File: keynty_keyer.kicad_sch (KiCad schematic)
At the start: 0 parts

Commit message: added power conditioning
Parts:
- added BT1: 9V Alkaline, symbol Device:Battery_Cell
- added C1: 100u, symbol Device:C_Polarized
- added R1: 47, symbol Device:R
- added SW1: Power, symbol Switch:SW_SPST
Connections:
- new net: BT1.1 (+), SW1.1 (A)
- new net: R1.1, SW1.2 (B)
- new net GND: BT1.2 (-), C1.2
- new net VCC: C1.1, R1.2

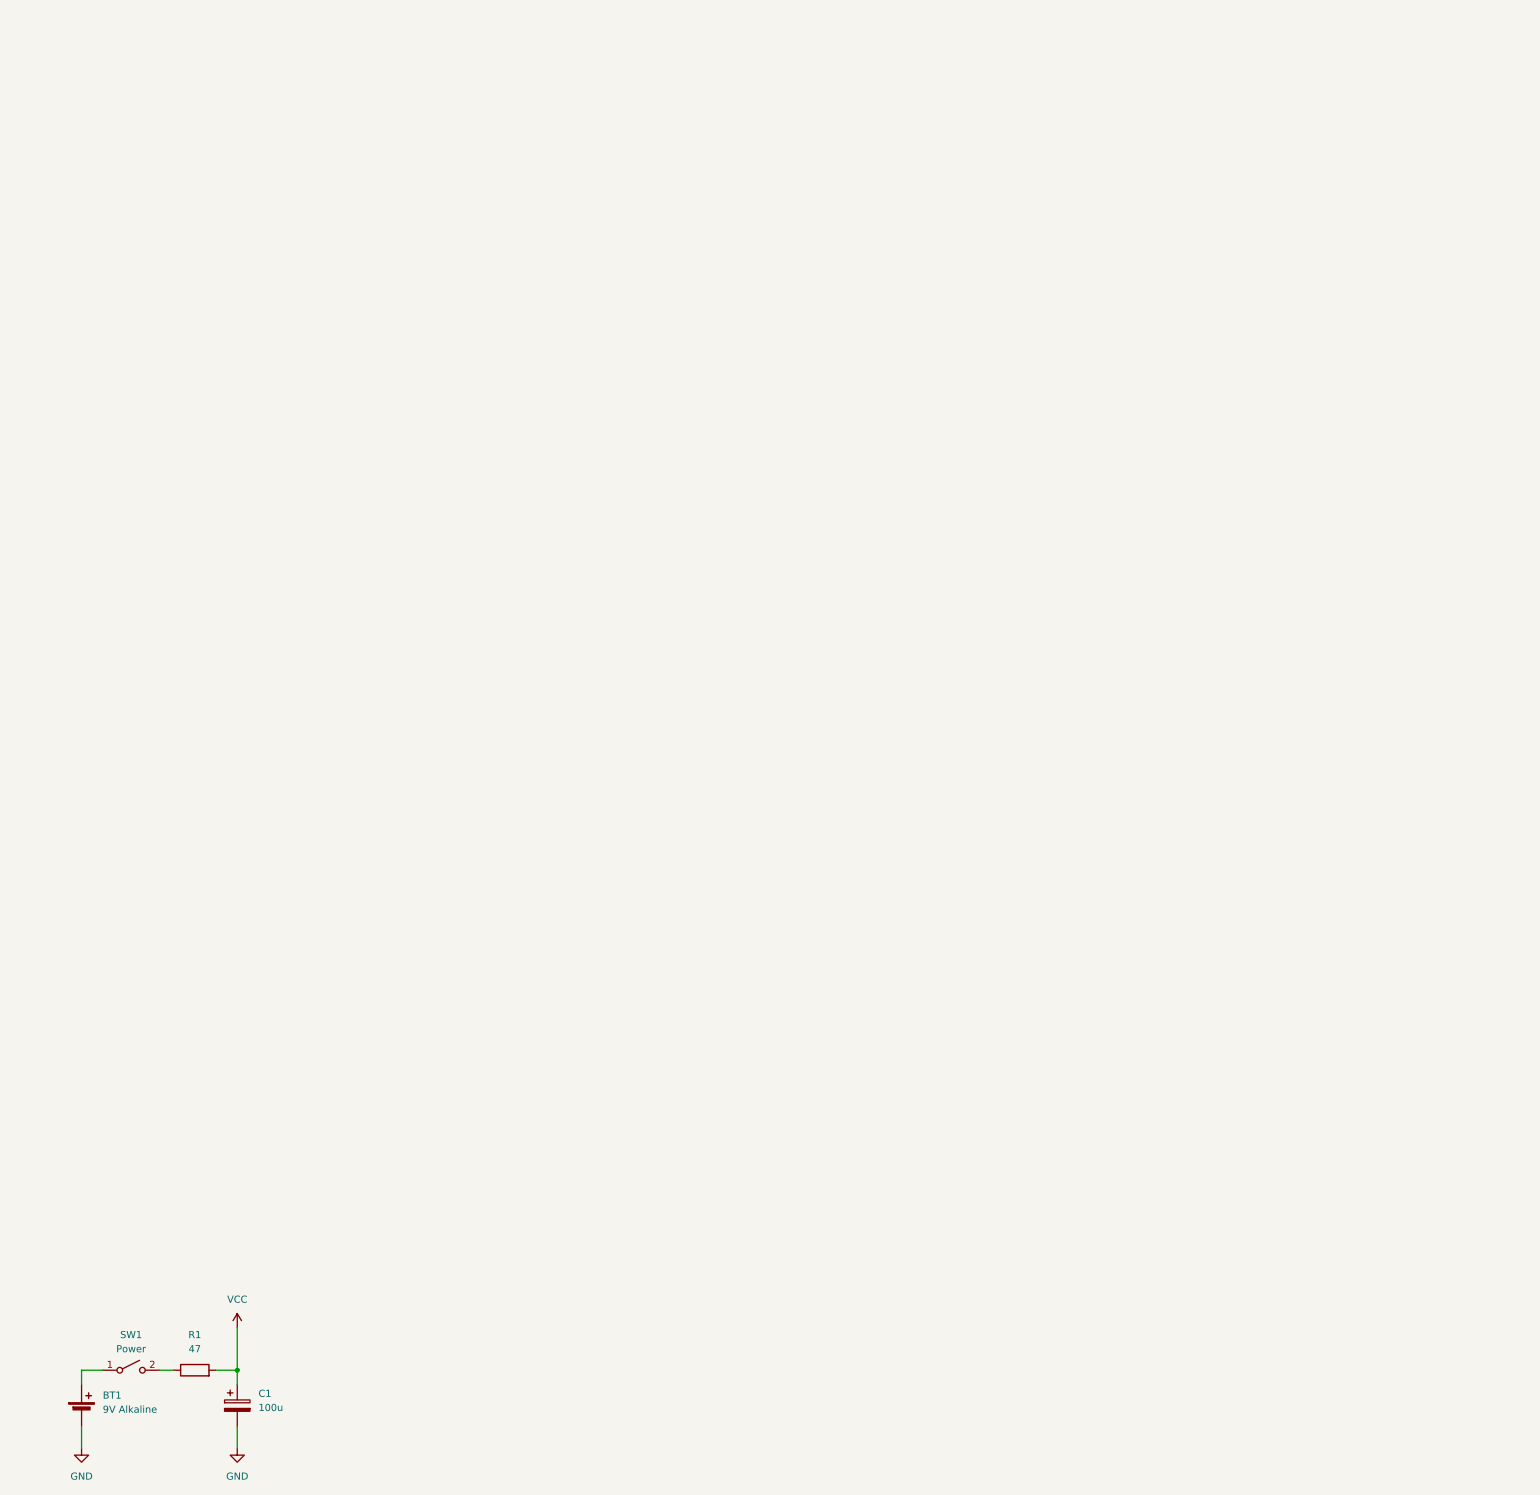
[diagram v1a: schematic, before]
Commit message: First Draft of schematic, starting from minty keyer, removed all the diode logic, changed output and input stages
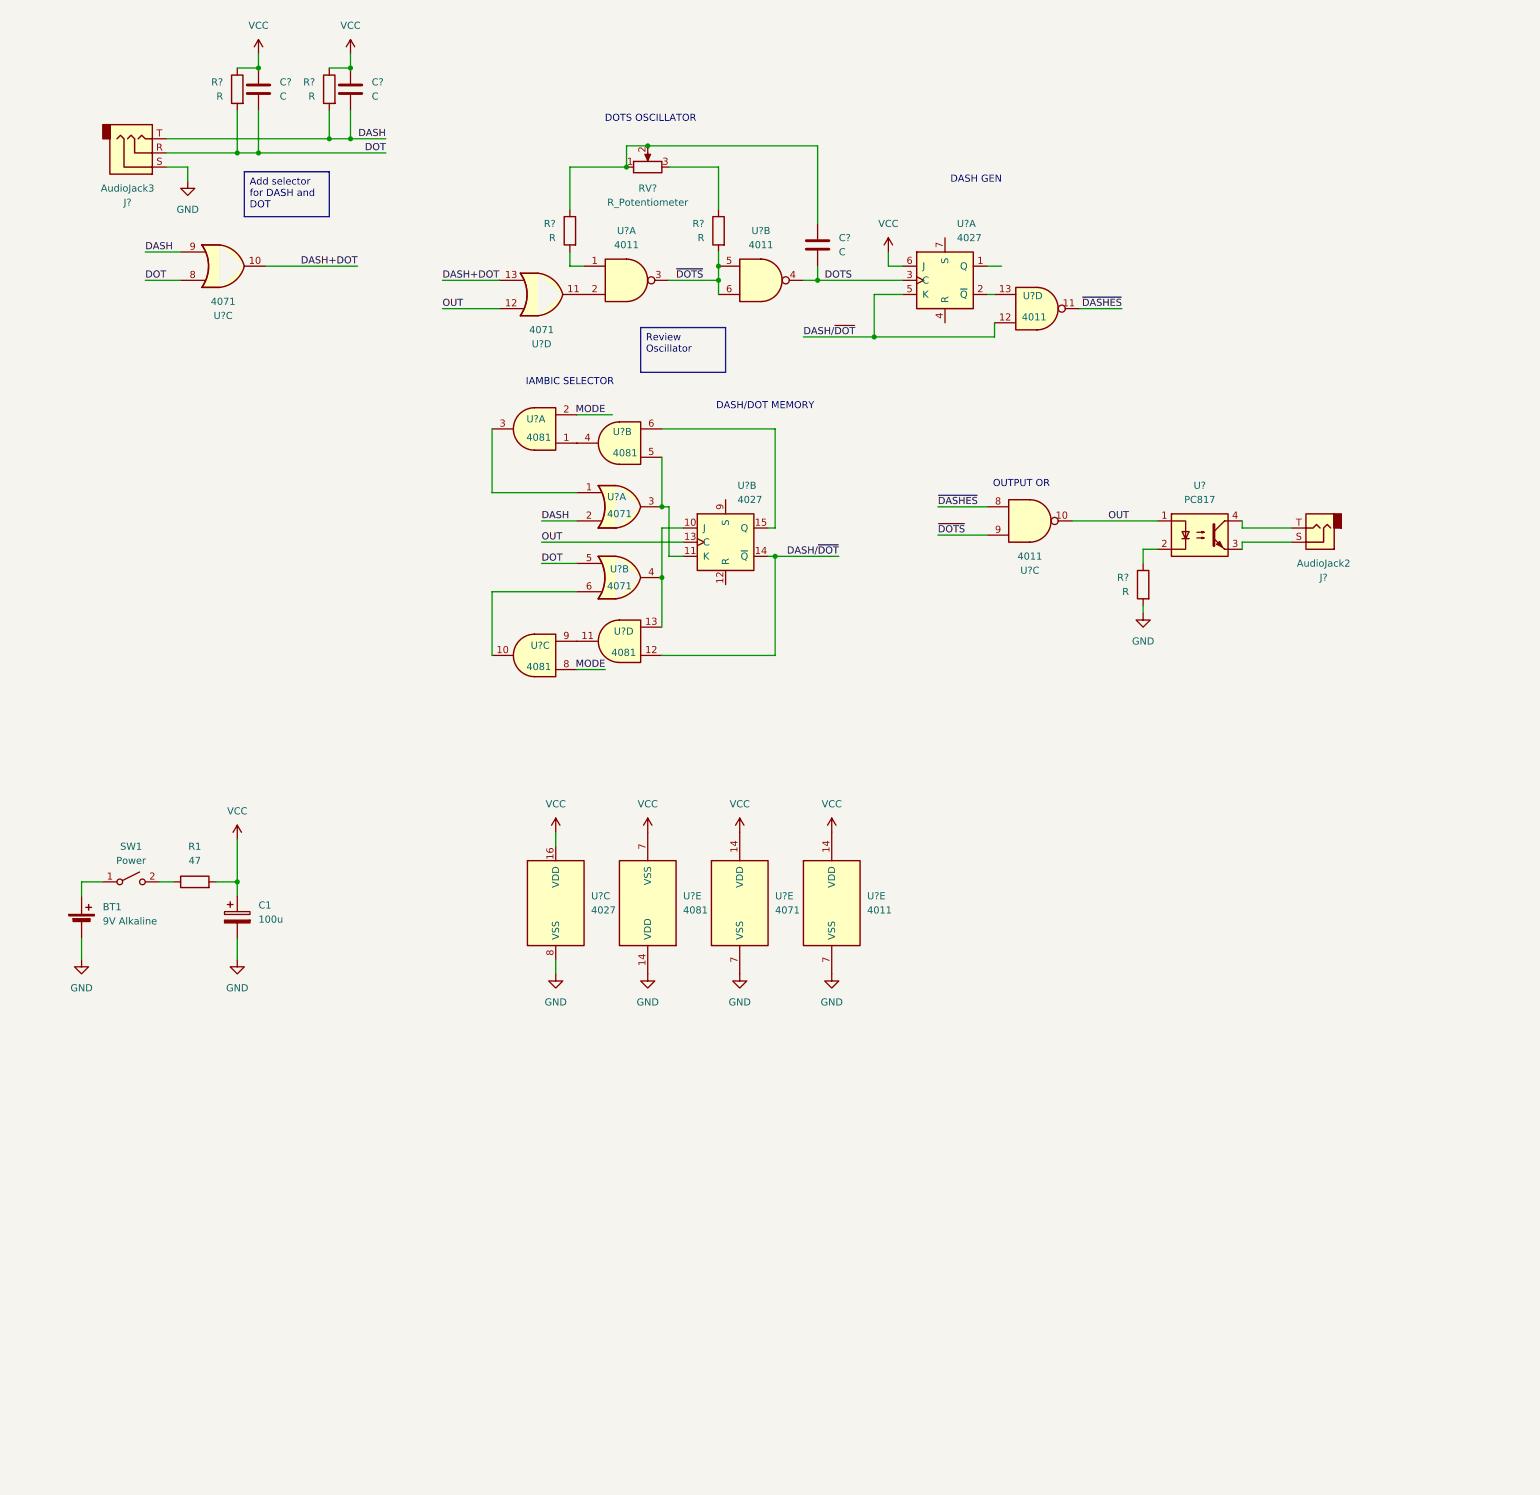
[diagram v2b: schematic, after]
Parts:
- added C? (x3): C, symbol Device:C
- added J?: AudioJack3, symbol Connector_Audio:AudioJack3
- added J?: AudioJack2, symbol Connector_Audio:AudioJack2
- added R? (x5): R, symbol Device:R
- added RV?: R_Potentiometer, symbol Device:R_Potentiometer
- added U? (x5): 4081, symbol 4xxx:4081
- added U? (x5): 4011, symbol 4xxx:4011
- added U? (x3): 4027, symbol 4xxx:4027
- added U?: PC817, Package_DIP:DIP-4_W7.62mm_LongPads, symbol Isolator:PC817
- added U? (x5): 4071, symbol 4xxx:4071
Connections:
- net GND: now also J?.S, R?.2, U?.14 (VDD), U?.7 (VSS), U?.7 (VSS), U?.8 (VSS)
- net VCC: now also C?.1, C?.1, R?.1, R?.1, U?.14 (VDD), U?.14 (VDD), U?.16 (VDD), U?.6 (J), U?.7 (VSS)
- new net: C?.1, R?.1, RV?.1, RV?.2
- new net: U?.13, U?.2 (~{Q})
- new net: U?.10 (J), U?.13, U?.4
- new net: U?.11 (K), U?.3, U?.5
- new net: U?.15 (Q), U?.6
- new net: R?.2, U?.1
- new net: R?.1, U?.2
- new net: J?.S, U?.3
- new net: J?.T, U?.4
- new net: U?.1, U?.4
- new net: U?.1, U?.3
- new net: U?.10, U?.6
- new net: U?.11, U?.9
- new net: U?.11, U?.2
- new net: R?.1, RV?.3
- new net DASH: C?.2, J?.T, R?.2, U?.2, U?.9
- new net DASH+DOT: U?.10, U?.13
- new net DASH/~{DOT}: U?.12, U?.12, U?.14 (~{Q}), U?.5 (K)
- new net DOT: C?.2, J?.R, R?.2, U?.5, U?.8
- new net DOTS: C?.2, U?.3 (C), U?.4
- new net MODE: U?.2, U?.8
- new net OUT: U?.1, U?.10, U?.12, U?.13 (C)
- new net ~{DASHES}: U?.11, U?.8
- new net ~{DOTS}: R?.2, U?.3, U?.5, U?.6, U?.9
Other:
- note added: "DASH GEN"
- note added: "DASH/DOT MEMORY"
- note added: "DOTS OSCILLATOR"
- note added: "IAMBIC SELECTOR"
- note added: "OUTPUT OR"
- moved on the sheet: BT1, C1, R1, SW1

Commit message: added selector dot/dash, verified oscillator frequencies, added buzzer placeholder
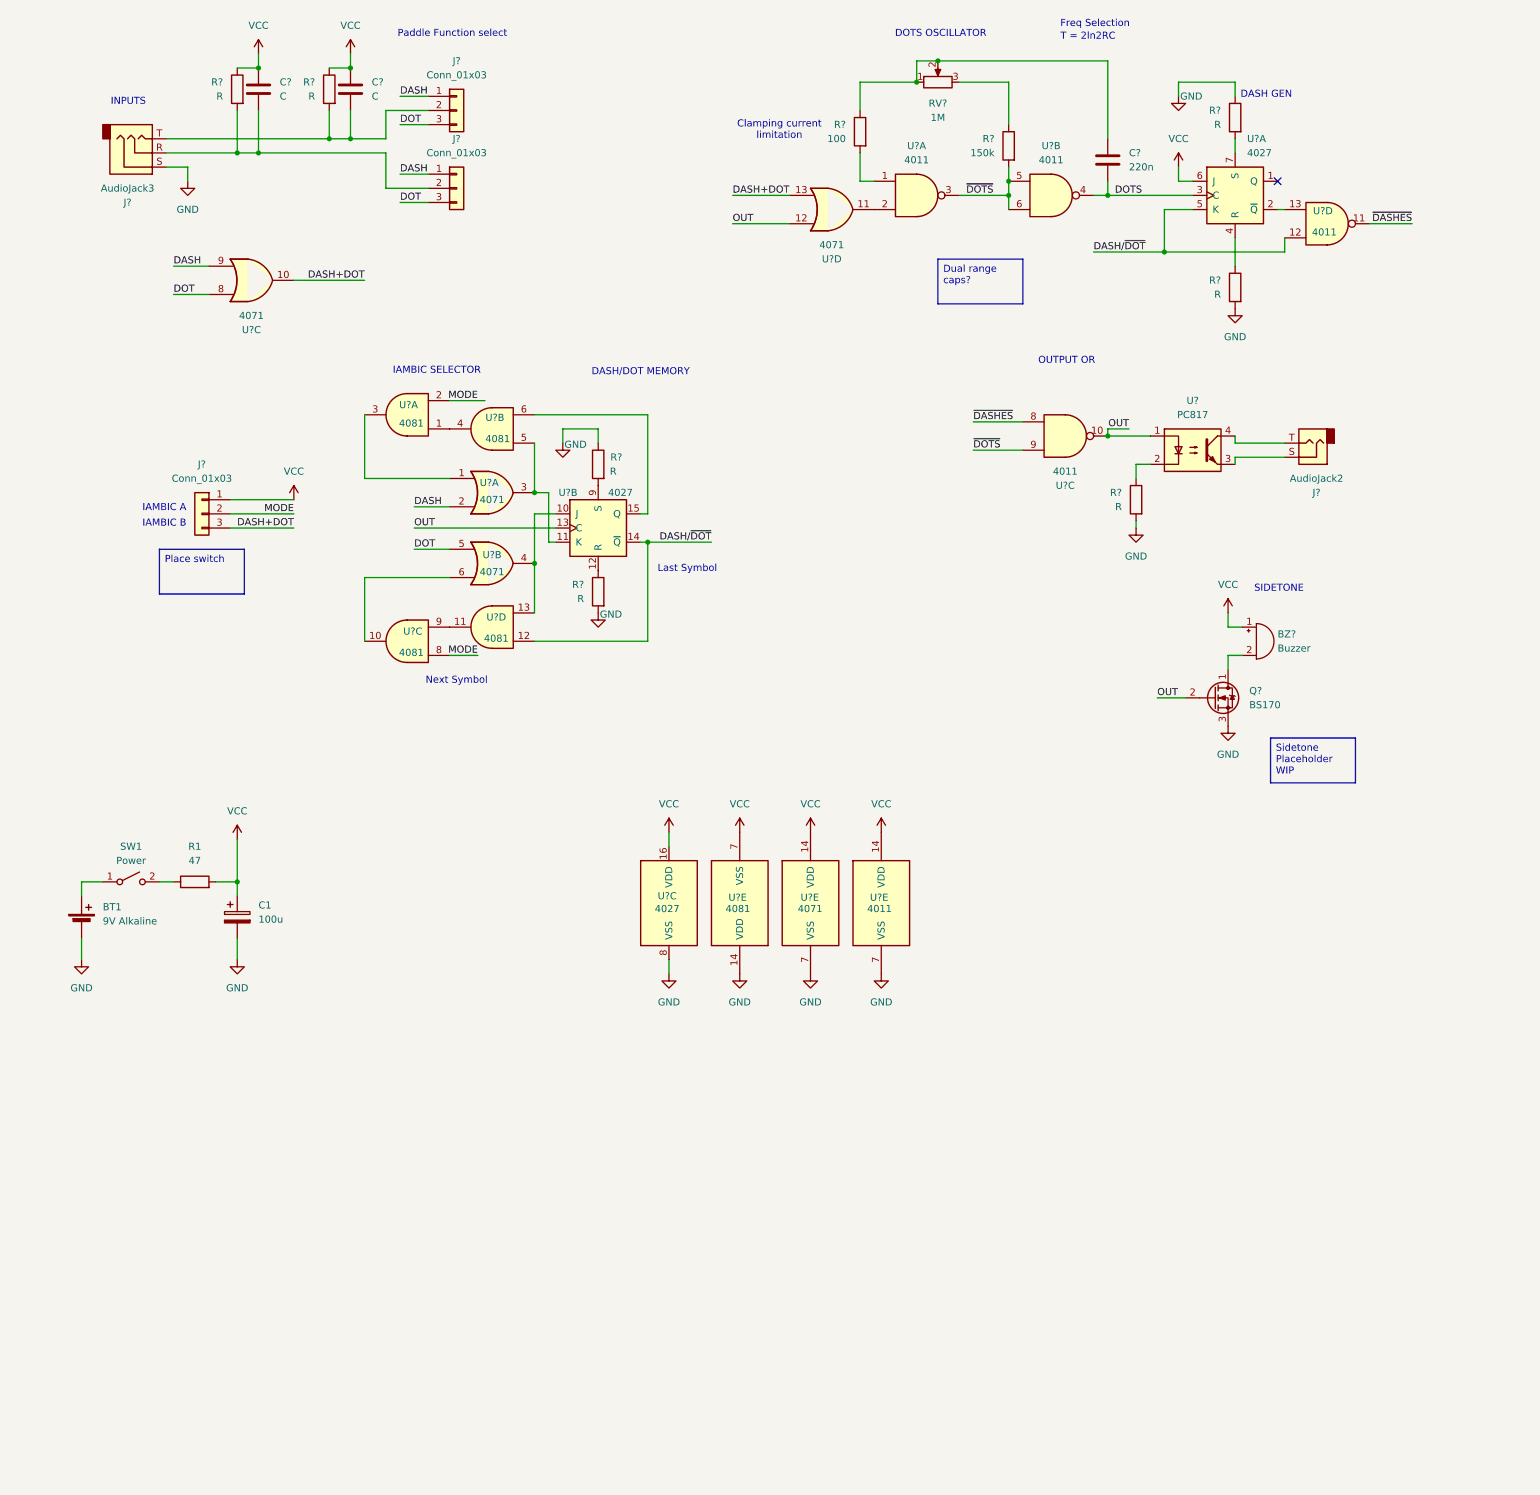
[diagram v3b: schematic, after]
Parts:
- removed R?: R, symbol Device:R
- added BZ?: Buzzer, symbol Device:Buzzer
- added J? (x3): Conn_01x03, symbol Connector_Generic:Conn_01x03
- added Q?: BS170, Package_TO_SOT_THT:TO-92_Inline, symbol Transistor_FET:BS170
- added R? (x4): R, symbol Device:R
- added R?: 100, symbol Device:R
- C?: value C -> 220n
- R?: value R -> 150k
- RV?: value R_Potentiometer -> 1M
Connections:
- net DASH: now also J?.1 (Pin_1), J?.1 (Pin_1); no longer C?.2, J?.T, R?.2
- net DASH+DOT: now also J?.3 (Pin_3)
- net DOT: now also J?.3 (Pin_3), J?.3 (Pin_3); no longer C?.2, J?.R, R?.2
- net GND: now also Q?.3 (S), R?.1, R?.1, R?.2, R?.2
- net MODE: now also J?.2 (Pin_2)
- net OUT: now also Q?.2 (G)
- net VCC: now also BZ?.1 (+), J?.1 (Pin_1)
- net at C?.1, RV?.1, RV?.2: now also R?.1
- net at U?.12 (R): now also R?.1
- net at U?.9 (S): now also R?.2
- net at U?.1: now also R?.2
- net at U?.4 (R): now also R?.1
- net at U?.7 (S): now also R?.2
- new net: BZ?.2 (-), Q?.1 (D)
- new net: C?.2, J?.2 (Pin_2), J?.T, R?.2
- new net: C?.2, J?.2 (Pin_2), J?.R, R?.2
- no-connect marks 0 -> 1
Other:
- note added: "Clamping current limitation"
- note added: "Freq Selection"
- note added: "IAMBIC A"
- note added: "IAMBIC B"
- note added: "INPUTS"
- note added: "Last Symbol"
- note added: "Next Symbol"
- note added: "Paddle Function select"
- note added: "SIDETONE"
- note added: "T = 2ln2RC"
- moved on the sheet: C?, J?, R?, RV?, U?, U?A, U?B, U?C, U?D, U?E
